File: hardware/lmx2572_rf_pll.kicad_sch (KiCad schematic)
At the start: 38 parts, among them U2 LMX2572RHAT

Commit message: Completed schematics
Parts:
- removed C11, C15, C16, C6, C9: 1u, Capacitor_SMD:C_0603_1608Metric, symbol Device:C_Small
- removed C7: 100n, Capacitor_SMD:C_0402_1005Metric, symbol Device:C_Small
- removed R1, R10, R2, R3, R4, R5, R6, R9: 0R, Resistor_SMD:R_0402_1005Metric, symbol Device:R_Small_US
- removed R12: 4K7, Resistor_SMD:R_0402_1005Metric, symbol Device:R_Small_US
- removed R3_LF, R4_LF: 0R, Resistor_SMD:R_0603_1608Metric, symbol Device:R_Small_US
- removed R7, R8: 51R, Resistor_SMD:R_0402_1005Metric, symbol Device:R_Small_US
- added C28, C30, C31, C32, C33, C34: 1u, Capacitor_SMD:C_0402_1005Metric, symbol Device:C_Small
- added C29, C43: 100n, Capacitor_SMD:C_0402_1005Metric, symbol Device:C_Small
- added FB2, FB4: 180R, Inductor_SMD:L_0402_1005Metric, symbol Device:FerriteBead_Small
- added R15, R16: 49R9, Resistor_SMD:R_0402_1005Metric, symbol Device:R_Small
- added R27, R28, R33, R34, R35, R43: 0R, Resistor_SMD:R_0402_1005Metric, symbol Device:R_Small
- added R3: 10k, Resistor_SMD:R_0402_1005Metric, symbol Device:R_Small
- C10: MFN MBAST105SB7103KFNA18 -> (none); MPN (none) -> C0402C103K4RECTU; Manufacturer Taiyo Yuden -> KEMET; SPN 963-MBAST105SB7103KF -> 399-C0402C103K4RECTUCT-ND; Supplier Mouser -> Digikey; Voltage 25V -> 16V
- C12: footprint Capacitor_SMD:C_0603_1608Metric -> Capacitor_SMD:C_0402_1005Metric; C 10u -> 10uF; MPN MSASL168BB5106KTNB33 -> GRM155R61A106ME11D; Manufacturer Taiyo Yudon -> Murata Electronics; SPN (none) -> 490-GRM155R61A106ME11DCT-ND; Supplier (none) -> Digikey; Tolerance 10% -> 20%; Voltage 10V -> 10v
- C13, C14: value 1u -> 10u; footprint Capacitor_SMD:C_0603_1608Metric -> Capacitor_SMD:C_0402_1005Metric; C 1u -> 10uF; Dielectric X7R -> X5R; MPN MBASG168AB7105KTNA01 -> GRM155R61A106ME11D; Manufacturer Taiyo Yudon -> Murata Electronics; SPN (none) -> 490-GRM155R61A106ME11DCT-ND; Supplier (none) -> Digikey; Tolerance 10% -> 20%; Voltage 35V -> 10v
- C17: footprint Capacitor_SMD:C_0603_1608Metric -> Capacitor_SMD:C_0402_1005Metric; C 1u -> 1uF; Dielectric X7R -> X5R; MPN MBASG168AB7105KTNA01 -> EMK105BJ105KV-F; SPN (none) -> 587-2477-1-ND; Supplier (none) -> Digikey; Voltage 35V -> 16V
- C18, C19, C20: MFN MBAST105SB7104KFNA18 -> (none); MPN (none) -> CL05B104KA5NNNC; Manufacturer Taiko Yuden -> Samsung Electro-Mechanics; SPN 963-MBAST105SB7104KF -> 1276-6720-1-ND; Supplier Mouser -> Digikey
- C1_LF?: renamed from C1_LF1; now not fitted
- C21, C22, C23, C24: MFN 520L103KT16 -> (none); MPN (none) -> 520L103KT16T; SPN 581-520L103KT16 -> 1284-1540-1-ND; Supplier Mouser -> Digikey
- C2_LF: footprint Resistor_SMD:R_0603_1608Metric -> Capacitor_SMD:C_0603_1608Metric; MPN (none) -> C1608C0G1V153J080AC; Manufacturer (none) -> TDK Corporation; SPN (none) -> 445-174557-1-ND; Supplier (none) -> Digikey
- C3_LF: now not fitted
- C4_LF: MPN (none) -> GCM1885C1H222JA16J; Manufacturer (none) -> Murata Electronics; SPN (none) -> 490-GCM1885C1H222JA16JCT-ND; Supplier (none) -> Digikey
- R2_LF?: renamed from R2_LF1; footprint Resistor_SMD:R_0603_1608Metric -> Resistor_SMD:R_0402_1005Metric; symbol Device:R_Small_US -> Device:R_Small; MPN (none) -> RC0402JR-07330RL; Manufacturer (none) -> YAGEO; SPN (none) -> 311-330JRCT-ND; Supplier (none) -> Digikey
- renumbered U2 to U?
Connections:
- net 3V3_PLL: now also C17.1, U?.11 (VCCCP), U?.15 (VCCMASH), U?.26 (VCCVCO2), U?.37 (VCCVCO), U?.7 (VCCDIG), C30.1, C31.1, C32.1, C33.1, FB4.2
- net 3V3_PLL_RF: now also C18.1, U?.21 (VCCBUF), FB2.2
- net GND: now also C28.2, C29.1, C30.2, C31.2, C32.2, C33.2, C34.2, C43.1, R15.1, R16.1, R3.1
- net REF_OSC_N: now also R16.2, R35.1
- net REF_OSC_P: now also R15.2, R43.1
- net lmx2572.ce: now also R3.2
- net lmx2572.sync: now also R33.2; no longer U?.5 (SYNC)
- net at C20.1: now also R43.2; no longer U?.9 (OSCINM)
- net at C20.2: now also U?.9 (OSCINM)
- net at C3_LF.1: now also R27.2, R28.1
- net at U?.29 (VREFVCO2): now also C13.1
- net at C14.1: now also U?.33 (VBIASVARAC); no longer U?.7 (VCCDIG)
- net at C1_LF?.1, C2_LF.1, U?.12 (CPOUT): now also R27.1
- net at U?.27 (VBIASVCO2): now also C43.2
- net at C19.2: now also U?.8 (OSCINP)
- net at U?.10 (VREGIN): now also C34.1
- net at C4_LF.1, U?.35 (VTUNE): now also R28.2
- net at C19.1: now also R35.2; no longer U?.8 (OSCINP)
- new net: R33.1, U?.5 (SYNC)
- new net 3V3: C28.1, C29.2, FB2.1, FB4.1
- new net pll_sync_ext: R34.2
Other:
- company: (none) -> ${COMPANY}
- title: (none) -> LMX2572 RF SYNTHESIZER
- moved on the sheet: C10, C12, C17, C18, C21, C2_LF, C4_LF, C8, U?

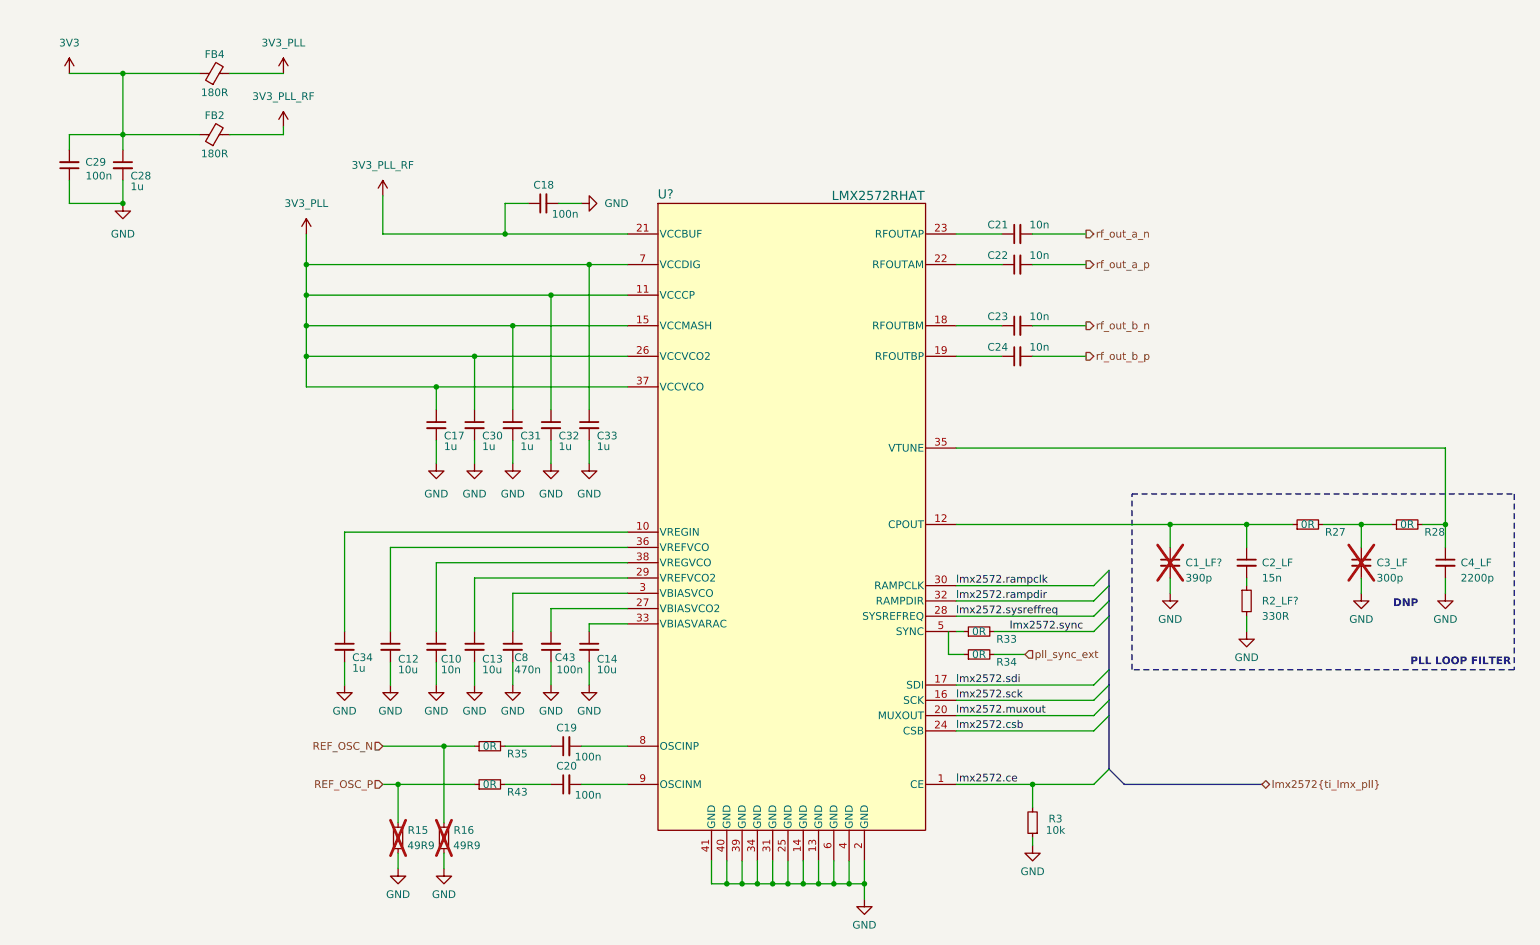
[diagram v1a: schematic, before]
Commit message: Completed core PCB routing
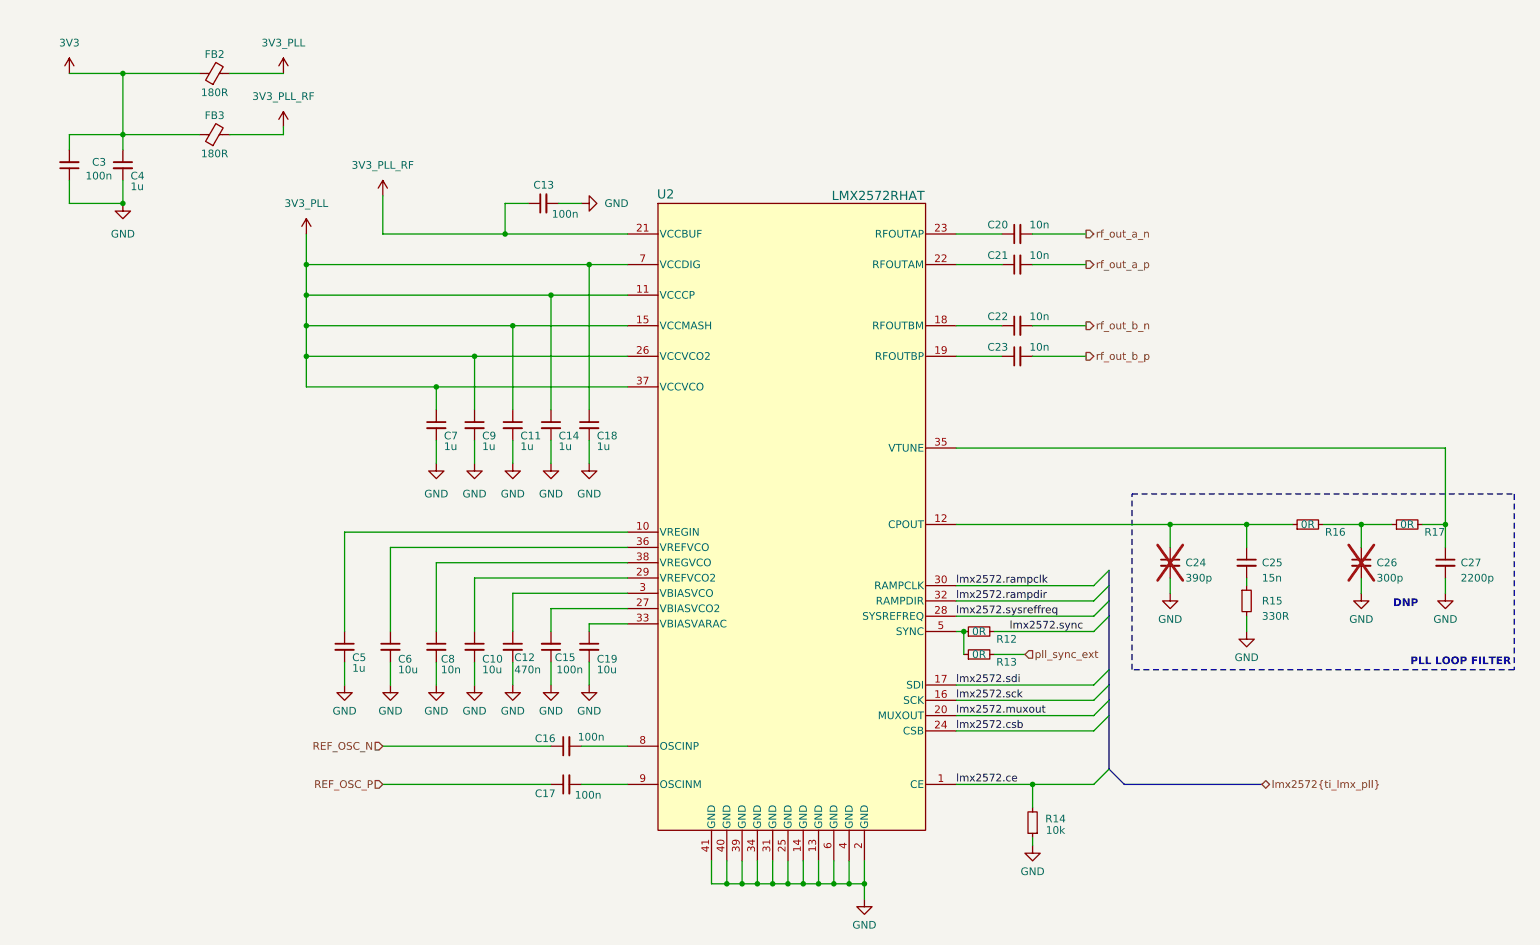
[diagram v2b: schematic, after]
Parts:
- removed R15, R16: 49R9, Resistor_SMD:R_0402_1005Metric, symbol Device:R_Small
- removed R35, R43: 0R, Resistor_SMD:R_0402_1005Metric, symbol Device:R_Small
- C24: renamed from C1_LF?; footprint Resistor_SMD:R_0603_1608Metric -> Capacitor_SMD:C_0402_1005Metric
- C25: renamed from C2_LF; footprint Capacitor_SMD:C_0603_1608Metric -> Capacitor_SMD:C_0402_1005Metric; MPN C1608C0G1V153J080AC -> C0402C153J4RACTU; Manufacturer TDK Corporation -> KEMET; SPN 445-174557-1-ND -> 80-C0402C153J4R; Supplier Digikey -> Mouser
- C26: renamed from C3_LF; footprint Resistor_SMD:R_0603_1608Metric -> Capacitor_SMD:C_0402_1005Metric
- C27: renamed from C4_LF; footprint Resistor_SMD:R_0603_1608Metric -> Capacitor_SMD:C_0402_1005Metric; MPN GCM1885C1H222JA16J -> VJ0402Y222JXXAC; SPN 490-GCM1885C1H222JA16JCT-ND -> 77-VJ0402Y222JXXAC; Supplier Digikey -> Mouser
- U2: renamed from U?; footprint RHA0040H -> sigma0_Packages_QFN:RHA0040H; MPN (none) -> LMX2572RHAT; Manufacturer (none) -> Texas Instruments; SPN (none) -> 296-47540-1-ND; Supplier (none) -> Digikey
- gave numbers to parts that had none: 1
- renumbered C13 to C10, C31 to C11, C8 to C12, C18 to C13, C32 to C14, C43 to C15, C19 to C16, C20 to C17, C33 to C18, C14 to C19, C21 to C20, C22 to C21, C23 to C22, C24 to C23, C29 to C3, C28 to C4, C34 to C5, C12 to C6, C17 to C7, C10 to C8, C30 to C9, FB4 to FB2, FB2 to FB3, R33 to R12, R34 to R13, R3 to R14, R27 to R16, R28 to R17
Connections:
- net REF_OSC_N: now also C16.1
- net REF_OSC_P: now also C17.1
- net at R13.1: now also R12.1, U2.5 (SYNC)

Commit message: Ready for FAB info
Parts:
- added C40: 100n, Capacitor_SMD:C_0402_1005Metric, symbol Device:C_Small
- added C41: 1u, Capacitor_SMD:C_0402_1005Metric, symbol Device:C_Small
- added TP2: TestPoint, TestPoint:TestPoint_THTPad_1.0x1.0mm_Drill0.5mm, symbol Connector:TestPoint
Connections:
- net 3V3: now also C40.2, C41.1
- net GND: now also C40.1, C41.2
- net at C27.1, R17.2, U2.35 (VTUNE): now also TP2.1
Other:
- moved on the sheet: C3, C4, FB2, FB3

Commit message: Sent off for quote
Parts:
- C12: MPN (none) -> MBAST168SB7474KTNA18; SPN 963-MBAST168SB7474KT -> 587-MBAST168SB7474KTNA18TR-ND; Supplier Mouser -> Digkey
- C24: MPN (none) -> GRM1555C1H391JA01D; Manufacturer (none) -> Murata Electronics; SPN (none) -> 490-1296-1-ND; Supplier (none) -> Digikey
- C26: MPN (none) -> GRM1555C1H301JA01D; Manufacturer (none) -> Murata Electronics; SPN (none) -> 490-3234-1-ND; Supplier (none) -> Digikey
- C8: MPN C0402C103K4RECTU -> 520L103KT16T; Manufacturer KEMET -> Kyocera Avx; SPN 399-C0402C103K4RECTUCT-ND -> 1284-1540-1-ND
- R16, R17: MPN (none) -> ERJ-2GE0R00X
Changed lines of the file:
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@@
 			)
 		)
-		(property "Description" "Resistor, small symbol"
+		(property "Description" "RES SMD 0 OHM JUMPER 1/10W 0402"
 			(at 229.87 101.6 0)
 			(effects
@@
 			)
 		)
+		(property "MPN" "ERJ-2GE0R00X"
+			(at 229.87 101.6 0)
+			(effects
+				(font
+					(size 1.27 1.27)
+				)
+				(hide yes)
+			)
+		)
 		(pin "1"
 		)
@@
 			)
 		)
-		(property "Description" "Unpolarized capacitor, small symbol"
+		(property "Description" "CAP CER 300PF 50V C0G/NP0 0402"
 			(at 238.76 107.95 0)
 			(effects
@@
 			)
 		)
-		(property "Manufacturer" ""
+		(property "Manufacturer" "Murata Electronics"
 			(at 238.76 107.95 0)
 			(effects
@@
 			)
 		)
-		(property "MPN" ""
+		(property "MPN" "GRM1555C1H301JA01D"
 			(at 238.76 107.95 0)
 			(effects
@@
 			)
 		)
-		(property "Supplier" ""
+		(property "Supplier" "Digikey"
 			(at 238.76 107.95 0)
 			(effects
@@
 			)
 		)
-		(property "SPN" ""
+		(property "SPN" "490-3234-1-ND"
 			(at 238.76 107.95 0)
 			(effects
@@
 			)
 		)
-		(property "Description" "Unpolarized capacitor, small symbol"
+		(property "Description" "CAP CER 0.47UF 25V X7R 0603"
 			(at 97.79 121.92 0)
 			(effects
@@
 			)
 		)
-		(property "Supplier" "Mouser"
+		(property "Supplier" "Digkey"
 			(at 97.79 121.92 0)
 			(effects
@@
 			)
 		)
-		(property "SPN" "963-MBAST168SB7474KT "
+		(property "SPN" "587-MBAST168SB7474KTNA18TR-ND"
 			(at 97.79 121.92 0)
 			(effects
@@
 			)
 		)
+		(property "MPN" "MBAST168SB7474KTNA18"
+			(at 97.79 121.92 0)
+			(effects
+				(font
+					(size 1.27 1.27)
+				)
+				(hide yes)
+			)
+		)
 		(pin "1"
 		)
@@
 			)
 		)
-		(property "Description" "Unpolarized capacitor, small symbol"
+		(property "Description" "CAP CER 390PF 50V C0G/NP0 0402"
 			(at 207.01 107.95 0)
 			(effects
@@
 			)
 		)
-		(property "Manufacturer" ""
+		(property "Manufacturer" "Murata Electronics"
 			(at 207.01 107.95 0)
 			(effects
@@
 			)
 		)
-		(property "MPN" ""
+		(property "MPN" "GRM1555C1H391JA01D"
 			(at 207.01 107.95 0)
 			(effects
@@
 			)
 		)
-		(property "Supplier" ""
+		(property "Supplier" "Digikey"
 			(at 207.01 107.95 0)
 			(effects
@@
 			)
 		)
-		(property "SPN" ""
+		(property "SPN" "490-1296-1-ND"
 			(at 207.01 107.95 0)
 			(effects
@@
 			)
 		)
-		(property "Description" "CAP CER 0402 10NF 16V X7R 10%"
+		(property "Description" "CAP CER 10000PF 16V X7R 0402"
 			(at 85.09 121.92 0)
 			(effects
@@
 			)
 		)
-		(property "Manufacturer" "KEMET"
+		(property "Manufacturer" "Kyocera Avx"
 			(at 85.09 121.92 0)
 			(effects
@@
 			)
 		)
-		(property "MPN" "C0402C103K4RECTU"
+		(property "MPN" "520L103KT16T"
 			(at 85.09 121.92 0)
 			(effects
@@
 			)
 		)
-		(property "SPN" "399-C0402C103K4RECTUCT-ND"
+		(property "SPN" "1284-1540-1-ND"
 			(at 85.09 121.92 0)
 			(effects
@@
 			)
 		)
-		(property "Description" "Resistor, small symbol"
+		(property "Description" "RES SMD 0 OHM JUMPER 1/10W 0402"
 			(at 246.38 101.6 0)
 			(effects
@@
 			(at 246.38 101.6 0)
 			(effects
+				(font
+					(size 1.27 1.27)
+				)
+				(hide yes)
+			)
+		)
+		(property "MPN" "ERJ-2GE0R00X"
+			(at 246.38 101.6 0)
+			(effects

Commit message: Updated firmware
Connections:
- net REF_OSC_N: now also C17.1; no longer C16.1
- net REF_OSC_P: now also C16.1; no longer C17.1
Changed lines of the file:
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@@
 	(hierarchical_label "REF_OSC_N"
 		(shape input)
-		(at 76.2 138.43 180)
+		(at 76.2 144.78 180)
 		(effects
 			(font
@@
 			)
 			(justify left)
-		)
-	)
-	(hierarchical_label "REF_OSC_P"
-		(shape input)
-		(at 76.2 144.78 180)
-		(effects
-			(font
-				(size 1.27 1.27)
-			)
-			(justify right)
 		)
 	)
@@
 		)
 	)
+	(hierarchical_label "REF_OSC_P"
+		(shape input)
+		(at 76.2 138.43 180)
+		(effects
+			(font
+				(size 1.27 1.27)
+			)
+			(justify right)
+		)
+	)
